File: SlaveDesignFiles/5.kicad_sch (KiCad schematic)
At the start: 43 parts

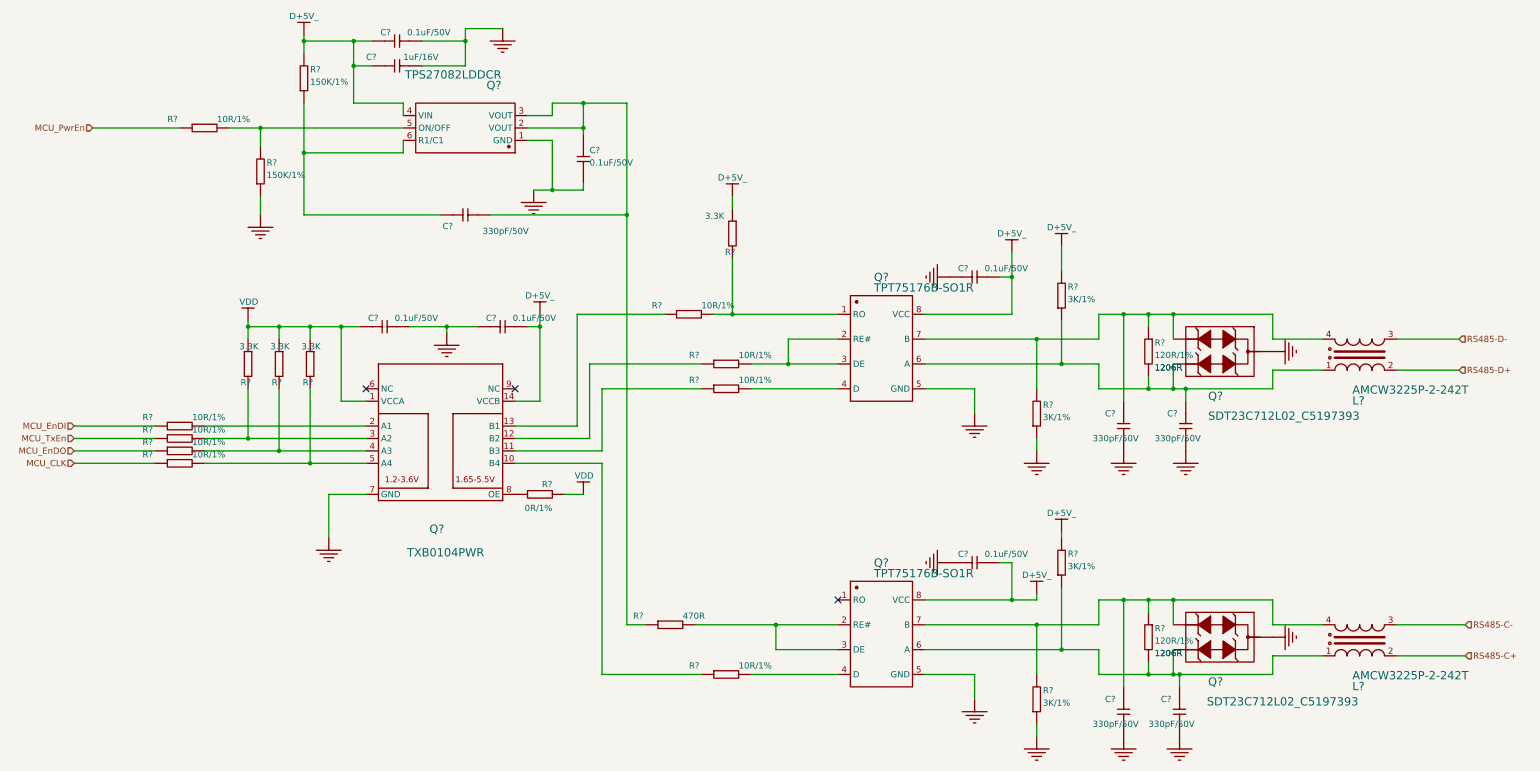
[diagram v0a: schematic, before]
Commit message: 1. 在USB处，修改了type-c5V输入的定义，添加了二极管；2. 将CJA1117B-3.3替换为AMS1117-3.3；3. 分配了testpoint的封装；4. 修改了H485，can插件的PE_GNG引脚定义。
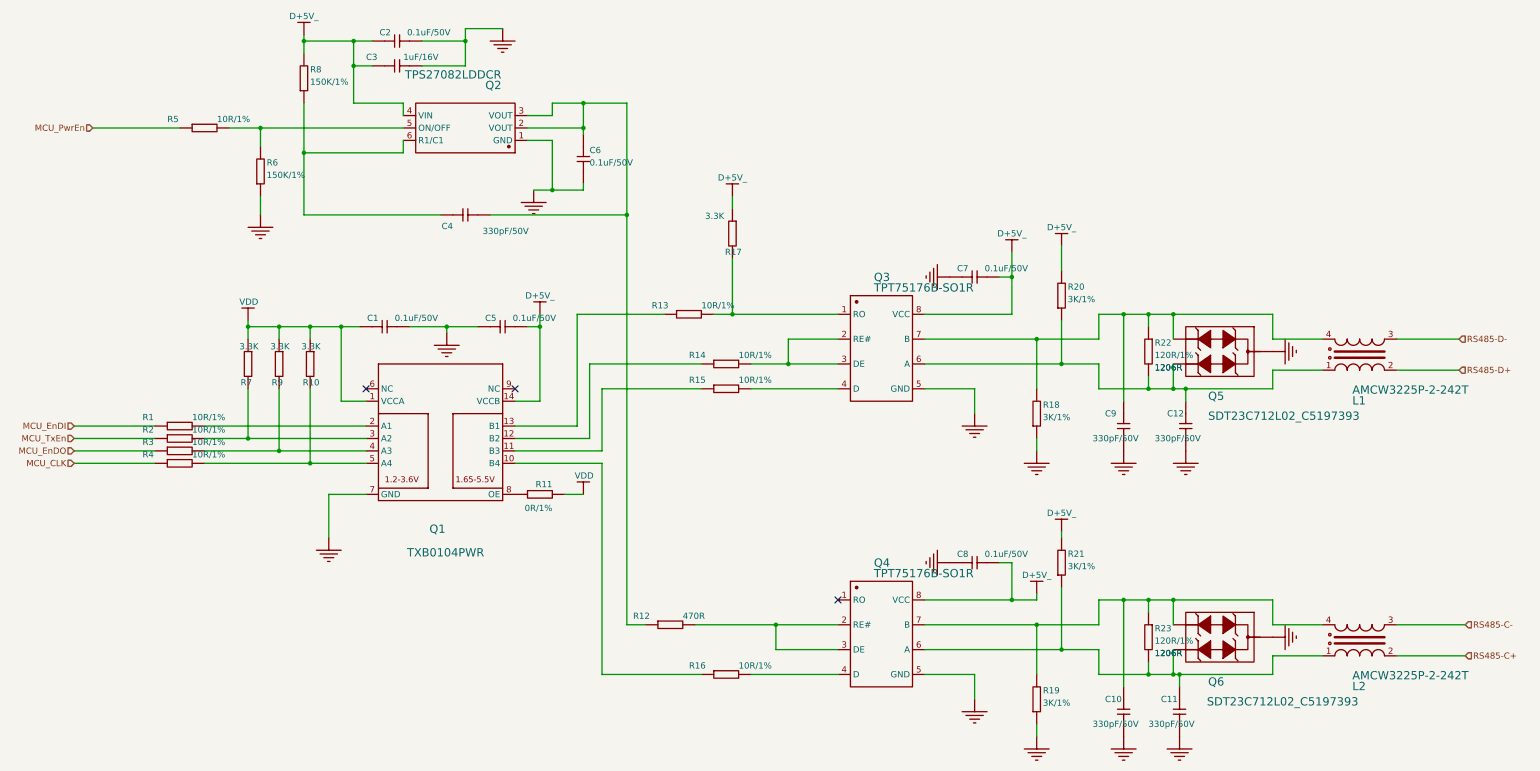
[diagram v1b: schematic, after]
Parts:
- gave numbers to parts that had none: 43

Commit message: Fix bugs in PWM subsheet
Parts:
- renumbered Q5 to D1, Q6 to D2
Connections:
- net D+5V_ renamed D+5V
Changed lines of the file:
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@@
 			)
 		)
-		(property "Value" "D+5V_"
+		(property "Value" "D+5V"
 			(at 270.51 180.34 0)
 			(effects
@@
 			)
 		)
-		(property "Value" "D+5V_"
+		(property "Value" "D+5V"
 			(at 275.59 109.22 0)
 			(effects
@@
 			)
 		)
-		(property "Value" "D+5V_"
+		(property "Value" "D+5V"
 			(at 168.91 123.19 0)
 			(effects
@@
 			(project "sheet1"
 				(path "/54840d93-b842-4275-b1cb-4ec5510cbfff/2459a240-a838-4f99-a8e3-bcddd2c7118f"
-					(reference "Q21")
+					(reference "Q15")
 					(unit 1)
 				)
 				(path "/54840d93-b842-4275-b1cb-4ec5510cbfff/7b6f65e6-43d5-48a0-9e5f-ee189406894e"
-					(reference "Q9")
+					(reference "Q7")
 					(unit 1)
 				)
 				(path "/54840d93-b842-4275-b1cb-4ec5510cbfff/d01706bf-c4a3-44ce-b4b0-8d63c3731b08"
-					(reference "Q15")
+					(reference "Q11")
 					(unit 1)
 				)
@@
 			(project "sheet1"
 				(path "/54840d93-b842-4275-b1cb-4ec5510cbfff/2459a240-a838-4f99-a8e3-bcddd2c7118f"
-					(reference "Q22")
+					(reference "Q16")
 					(unit 1)
 				)
 				(path "/54840d93-b842-4275-b1cb-4ec5510cbfff/7b6f65e6-43d5-48a0-9e5f-ee189406894e"
-					(reference "Q10")
+					(reference "Q8")
 					(unit 1)
 				)
 				(path "/54840d93-b842-4275-b1cb-4ec5510cbfff/d01706bf-c4a3-44ce-b4b0-8d63c3731b08"
-					(reference "Q16")
+					(reference "Q12")
 					(unit 1)
 				)
@@
 			(project "sheet1"
 				(path "/54840d93-b842-4275-b1cb-4ec5510cbfff/2459a240-a838-4f99-a8e3-bcddd2c7118f"
-					(reference "Q20")
+					(reference "Q14")
 					(unit 1)
 				)
 				(path "/54840d93-b842-4275-b1cb-4ec5510cbfff/7b6f65e6-43d5-48a0-9e5f-ee189406894e"
-					(reference "Q8")
+					(reference "Q6")
 					(unit 1)
 				)
 				(path "/54840d93-b842-4275-b1cb-4ec5510cbfff/d01706bf-c4a3-44ce-b4b0-8d63c3731b08"
-					(reference "Q14")
+					(reference "Q10")
 					(unit 1)
 				)
@@
 			)
 		)
-		(property "Value" "D+5V_"
+		(property "Value" "D+5V"
 			(at 265.43 110.49 0)
 			(effects
@@
 			)
 		)
-		(property "Value" "D+5V_"
+		(property "Value" "D+5V"
 			(at 275.59 167.64 0)
 			(effects
@@
 			(project "sheet1"
 				(path "/54840d93-b842-4275-b1cb-4ec5510cbfff/2459a240-a838-4f99-a8e3-bcddd2c7118f"
-					(reference "Q19")
+					(reference "Q13")
 					(unit 1)
 				)
 				(path "/54840d93-b842-4275-b1cb-4ec5510cbfff/7b6f65e6-43d5-48a0-9e5f-ee189406894e"
-					(reference "Q7")
+					(reference "Q5")
 					(unit 1)
 				)
 				(path "/54840d93-b842-4275-b1cb-4ec5510cbfff/d01706bf-c4a3-44ce-b4b0-8d63c3731b08"
-					(reference "Q13")
+					(reference "Q9")
 					(unit 1)
 				)
@@
 			)
 		)
-		(property "Value" "D+5V_"
+		(property "Value" "D+5V"
 			(at 120.65 66.04 0)
 			(effects
@@
 			)
 		)
-		(property "Value" "D+5V_"
+		(property "Value" "D+5V"
 			(at 208.28 99.06 0)
 			(effects
@@
 		(on_board yes)
 		(dnp no)
-		(property "Reference" "Q6"
+		(property "Reference" "D2"
 			(at 305.562 201.168 90)
 			(effects
@@
 			(project "sheet1"
 				(path "/54840d93-b842-4275-b1cb-4ec5510cbfff/2459a240-a838-4f99-a8e3-bcddd2c7118f"
-					(reference "Q24")
+					(reference "D8")
 					(unit 1)
 				)
 				(path "/54840d93-b842-4275-b1cb-4ec5510cbfff/7b6f65e6-43d5-48a0-9e5f-ee189406894e"
-					(reference "Q12")
+					(reference "D4")
 					(unit 1)
 				)
 				(path "/54840d93-b842-4275-b1cb-4ec5510cbfff/d01706bf-c4a3-44ce-b4b0-8d63c3731b08"
-					(reference "Q18")
+					(reference "D6")
 					(unit 1)
 				)
 				(path "/54840d93-b842-4275-b1cb-4ec5510cbfff/f5e14a6f-328f-4ef9-9718-0acdc1d336f8"
-					(reference "Q6")
+					(reference "D2")
 					(unit 1)
 				)
@@
 		(on_board yes)
 		(dnp no)
-		(property "Reference" "Q5"
+		(property "Reference" "D1"
 			(at 305.562 142.748 90)
 			(effects
@@
 			(project "sheet1"
 				(path "/54840d93-b842-4275-b1cb-4ec5510cbfff/2459a240-a838-4f99-a8e3-bcddd2c7118f"
-					(reference "Q23")
+					(reference "D7")
 					(unit 1)
 				)
 				(path "/54840d93-b842-4275-b1cb-4ec5510cbfff/7b6f65e6-43d5-48a0-9e5f-ee189406894e"
-					(reference "Q11")
+					(reference "D3")
 					(unit 1)
 				)
 				(path "/54840d93-b842-4275-b1cb-4ec5510cbfff/d01706bf-c4a3-44ce-b4b0-8d63c3731b08"
-					(reference "Q17")
+					(reference "D5")
 					(unit 1)
 				)
 				(path "/54840d93-b842-4275-b1cb-4ec5510cbfff/f5e14a6f-328f-4ef9-9718-0acdc1d336f8"
-					(reference "Q5")
+					(reference "D1")
 					(unit 1)
 				)
